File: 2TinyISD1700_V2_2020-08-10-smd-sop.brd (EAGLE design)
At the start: 45.5 x 48.3 mm, 18 parts, among them IC3 LM317MDT, U1 ATTINY4313-SU

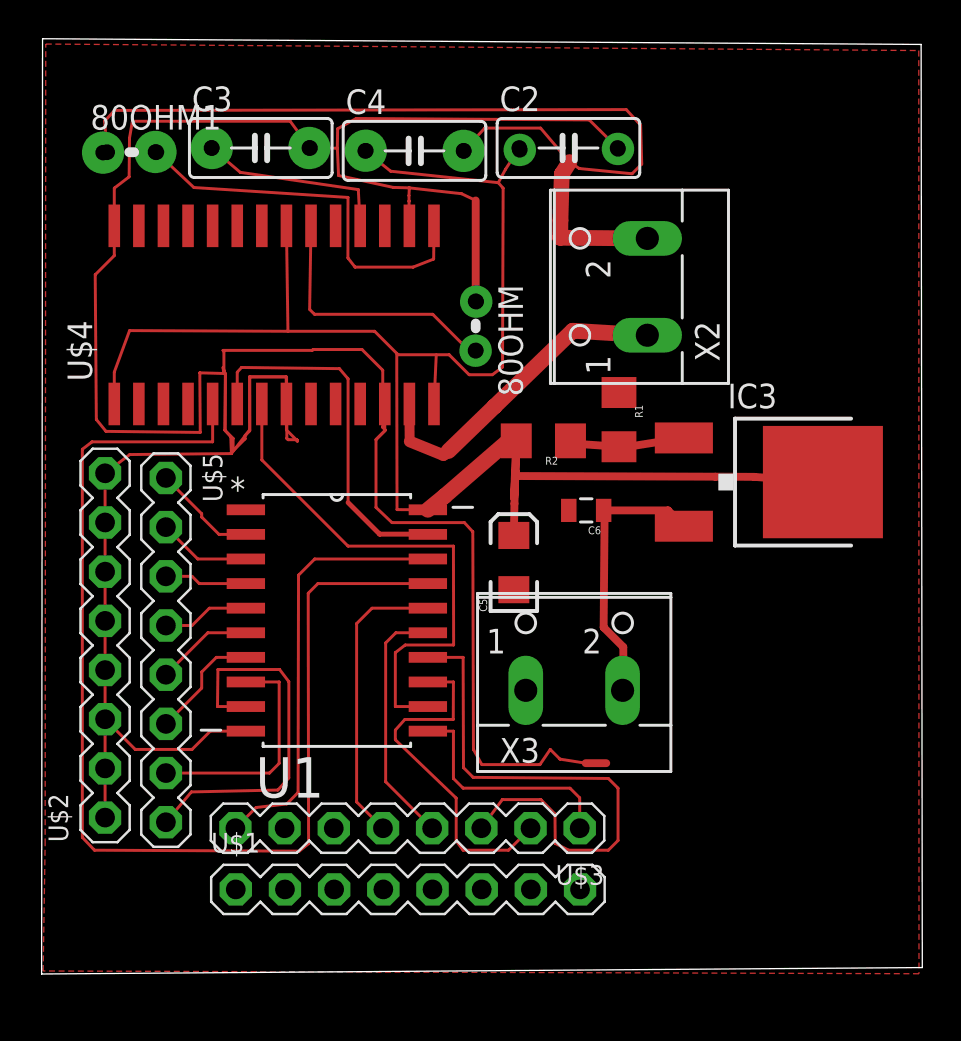
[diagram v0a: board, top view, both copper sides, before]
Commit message: added css connection
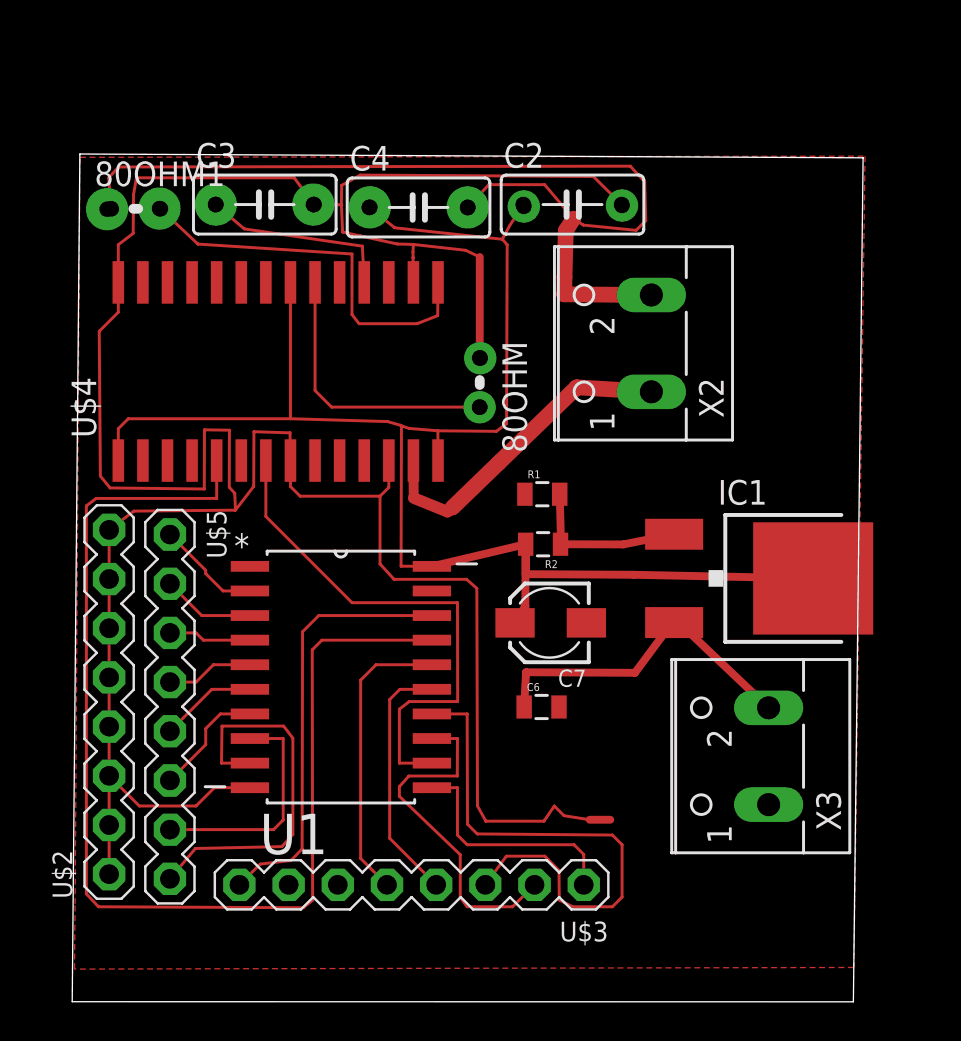
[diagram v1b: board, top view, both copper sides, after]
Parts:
- removed C5: (no value), SparkFun2:EIA3216
- removed IC3: LM317MDT, v-reg:DPACK
- removed U$1: 8PIN_HEADER, arduino:8PIN_HEADER
- added C7: 10UF 16V, Seeed-OPL-Capacitor:ELECTRO-SMD-A-3.8MM
- added IC1: LM317MDT, v-reg:DPACK
- R1, R2: device SparkFun:1206 -> SparkFun2:0805
- moved C6 10.4 mm to (23.8, 10.6), turned to 0 degrees
- moved X3 9.94 mm to (34.3, 8.07), turned to 90 degrees
- moved R1 5.52 mm to (23.9, 21.6), turned to 0 degrees
- moved R2 5.34 mm to (23.9, 19.0)
- moved 80OHM1 2.93 mm to (2.89, 36.3)
- moved C4 2.93 mm to (17.5, 36.4)
- moved U$5 2.93 mm to (4.65, 19.5)
- moved X2 2.93 mm to (28.2, 29.4)
- moved U$2 2.93 mm to (1.51, 1.98)
- moved U$3 2.93 mm to (26.0, 1.43)
- moved U1 2.93 mm to (13.5, 12.2)
- moved 80OHM 2.93 mm to (20.6, 27.4)
- moved U$4 2.93 mm to (10.2, 27.9)
- moved C2 2.93 mm to (25.4, 36.6)
- moved C3 2.93 mm to (9.55, 36.6)
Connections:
- removed net N$28: C6.1, IC3.3, X3.2
- new net 5V: C6.1, IC1.3, X3.2
- net CSK: no longer U$4.6
- net GND: now also C7.-; no longer C5.C, U$1.P$1, U$1.P$2, U$1.P$3, U$1.P$4, U$1.P$5, U$1.P$6, U$1.P$7, U$1.P$8
- net N$29: now also IC1.1; no longer IC3.1
- net VCC: now also C7.+, IC1.4; no longer C5.A, IC3.4
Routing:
- net GND: track 175.0 -> 150.8 mm
- net CSK: track 18.9 -> 0.00 mm
- net 5V: track 0.00 -> 17.8 mm
- net N$28: track 14.3 -> 0.00 mm
- net VCC: track 92.3 -> 84.3 mm
- net N$29: track 6.44 -> 8.51 mm
- net N$1: track 13.8 -> 14.4 mm
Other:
- board size 45.5 x 48.3 mm -> 40.8 x 43.8 mm
